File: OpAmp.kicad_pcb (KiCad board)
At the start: 2 copper layers, 47.5 x 26.5 mm, 47 parts, among them J1 Conn_01x05, J2 Conn_01x02, J3 Conn_01x02, J4 Conn_01x02, Q1 5551, Q10 5401, Q11 5551, Q12 5551, Q13 5551, Q14 5401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

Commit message: JLCPCB order 2021-04-11
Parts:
- removed C5: 100 nF, Capacitors_SMD:C_0805_HandSoldering
- removed D1, D2: D_x2_Serial_AKC, TO_SOT_Packages_SMD:SOT-23
- removed Q3, Q6: 5551, TO_SOT_Packages_SMD:SOT-23
- added R14: 680R, Resistors_SMD:R_0805_HandSoldering, F.Cu at (67.5, 70.2)
- added R15: 680R, Resistors_SMD:R_0805_HandSoldering, F.Cu at (62.4, 70.2)
- R2: value 330R -> 680R
- RV1: value 1k -> 2k
- moved Q8 5.08 mm to (72.3, 65.7)
- moved R6 4.99 mm to (72.6, 68.5), turned to 0 degrees
- moved R8 3.83 mm to (76.2, 61.5)
- moved Q10 3.68 mm to (77.5, 65.7), turned to 270 degrees
- moved Q1 3.50 mm to (67.0, 65.8)
- moved Q7 3.45 mm to (63.2, 65.8)
- moved R5 3.02 mm to (79.5, 61.5)
- moved R9 2.85 mm to (82.2, 66.8), turned to 0 degrees
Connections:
- Q1 pad 3: Net-(Q1-Pad3) -> Net-(C7-Pad1)
- Q7 pad 3: Net-(Q6-Pad2) -> Net-(Q2-Pad1)
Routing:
- net VCC: track 65.3 -> 45.9 mm, vias 12 -> 10
- net Net-(C5-Pad2): track 12.8 -> 0.00 mm
- net Net-(Q4-Pad3): track 5.46 -> 11.7 mm
- net Net-(Q7-Pad2): track 4.32 -> 10.0 mm
- net Net-(C7-Pad1): track 28.8 -> 34.0 mm
- net Net-(Q1-Pad2): track 3.75 -> 8.67 mm
- net Net-(C6-Pad1): track 21.3 -> 25.3 mm, vias 2 -> 0
- net Net-(Q10-Pad2): track 5.46 -> 1.94 mm
- net /NEG: track 13.9 -> 11.6 mm
- net VEE: track 46.0 -> 44.0 mm, vias 13 -> 12
- net /POS: track 16.4 -> 14.4 mm
- net Net-(Q6-Pad2): track 1.96 -> 0.00 mm
- net Net-(Q1-Pad3): track 1.91 -> 0.00 mm
- net Net-(D1-Pad2): track 1.89 -> 0.00 mm
- net Net-(Q12-Pad1): track 7.80 -> 8.88 mm
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
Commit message: Added partial outputs
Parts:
- removed J4: Conn_01x02, Pin_Headers:Pin_Header_Straight_1x02_Pitch2.54mm
- J1: value Conn_01x05 -> Conn_01x07; footprint Pin_Headers:Pin_Header_Straight_1x05_Pitch2.54mm -> Pin_Headers:Pin_Header_Straight_1x07_Pitch2.54mm
- moved R12 3.81 mm to (85.2, 79.0), turned to 90 degrees
- moved Q14 2.22 mm to (88.5, 78.7)
- moved Q16 1.32 mm to (79.5, 79.2)
- moved R13 0.66 mm to (82.8, 79.0), turned to 270 degrees
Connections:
- Q15 pad 2: Net-(Q15-Pad2) -> /DRVPLUS
- Q16 pad 2: Net-(J4-Pad2) -> /DRVMINUS
- R12 pad 1: Net-(Q15-Pad2) -> /DRVPLUS
- R13 pad 2: Net-(J4-Pad2) -> /DRVMINUS
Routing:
- net /DRVPLUS: track 0.00 -> 43.7 mm
- net /DRVMINUS: track 0.00 -> 41.0 mm
- net Net-(J4-Pad2): track 8.04 -> 0.00 mm
- net VEE: track 44.0 -> 37.8 mm
- net Net-(Q15-Pad2): track 5.23 -> 0.00 mm
- net /OUT: track 49.0 -> 44.4 mm
- net Net-(C6-Pad2): track 23.4 -> 24.2 mm
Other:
- board size 47.5 x 26.5 mm -> 48 x 28 mm
- board text added: "D+"
- board text added: "D-"

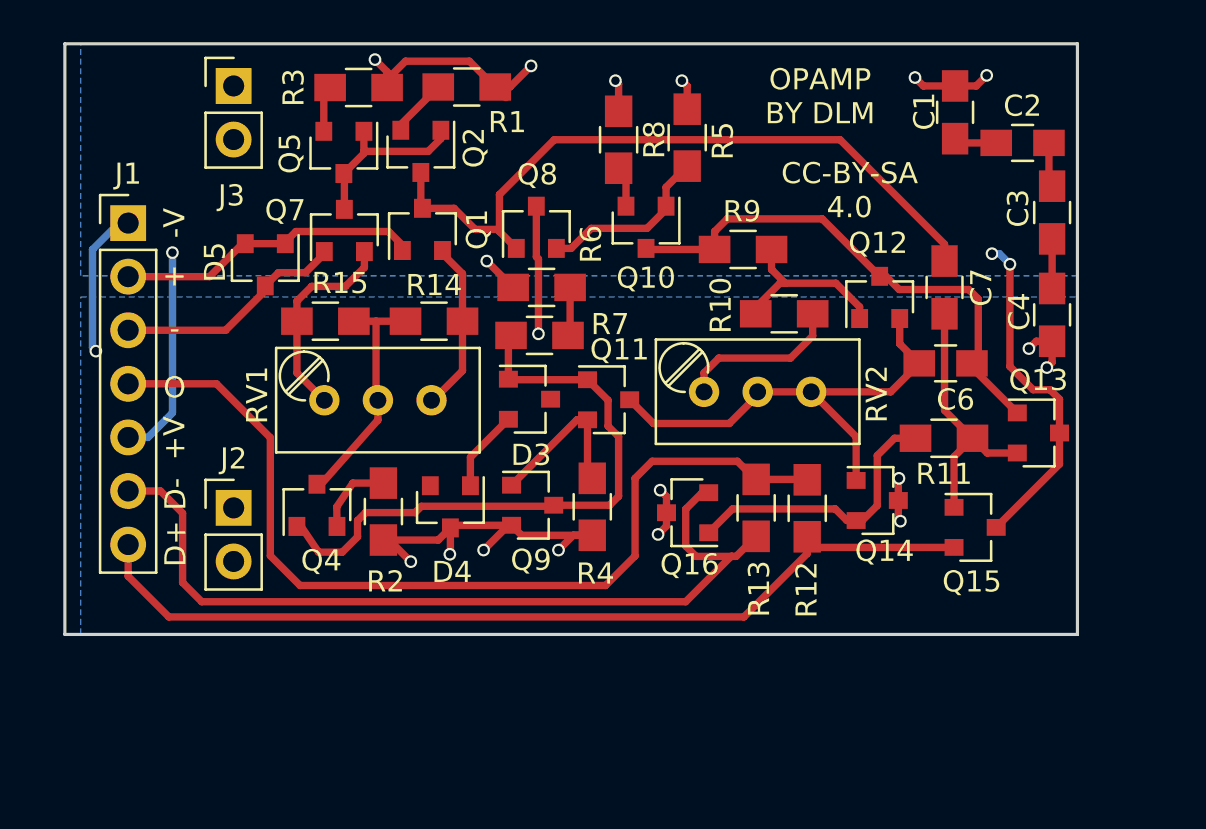
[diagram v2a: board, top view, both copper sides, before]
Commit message: Add spot for power transistors
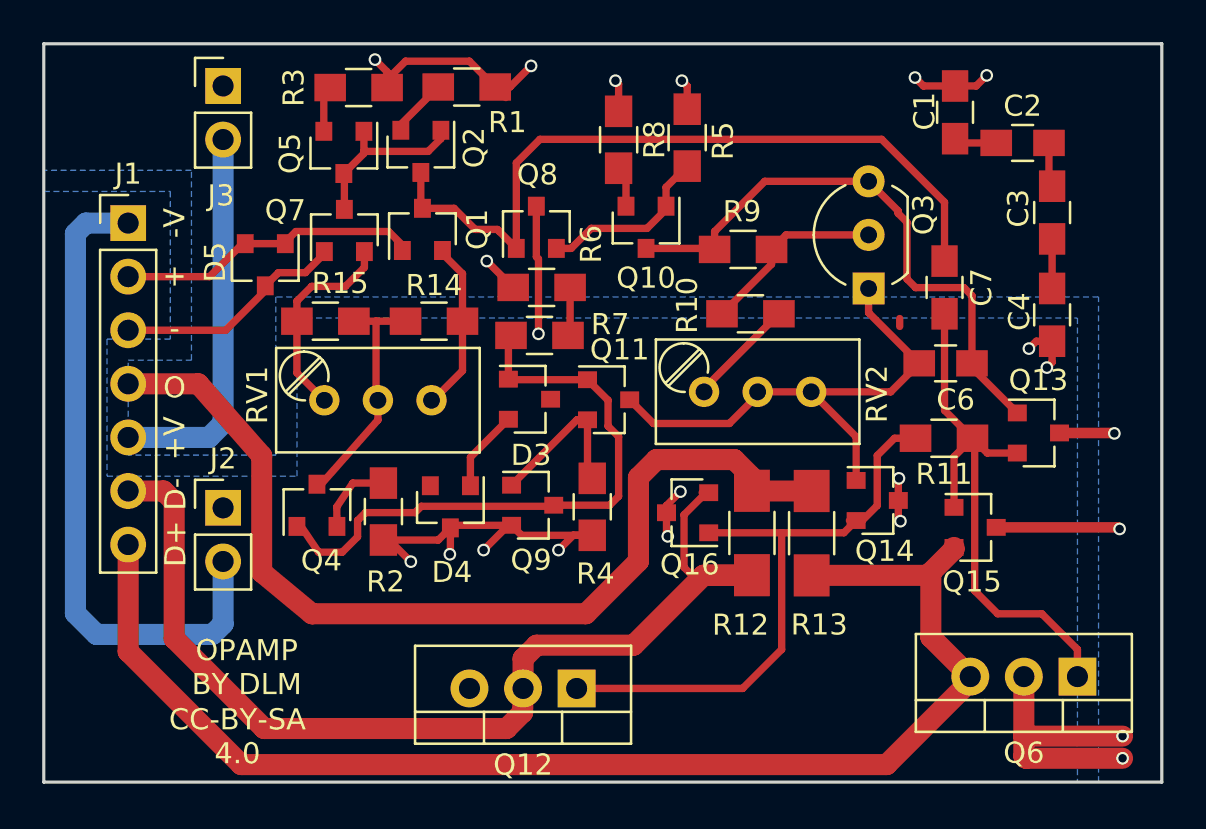
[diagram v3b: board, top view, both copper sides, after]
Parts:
- added Q3: 2N3904, TO_SOT_Packages_THT:TO-92_Inline_Wide, F.Cu at (88.1, 68.6)
- added Q6: TIP41, TO_SOT_Packages_THT:TO-220-3_Vertical, F.Cu at (98.0, 87.0)
- Q12: value 5551 -> TIP42; footprint TO_SOT_Packages_SMD:SOT-23 -> TO_SOT_Packages_THT:TO-220-3_Vertical
- R12, R13: footprint Resistors_SMD:R_0805_HandSoldering -> Resistors_SMD:R_1206_HandSoldering
- moved Q12 23.4 mm to (74.3, 87.6), turned to 180 degrees
- moved R10 1.60 mm to (82.5, 69.8)
- moved R13 1.21 mm to (82.6, 80.2)
- moved R12 1.20 mm to (85.4, 80.2)
- moved J2 0.50 mm to (57.5, 79.0)
- moved J3 0.50 mm to (57.5, 59.0)
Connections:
- Q12 pad 2: Net-(C6-Pad2) -> /DRVMINUS
- Q12 pad 3: Net-(C6-Pad1) -> VEE
- Q14 pad 2: Net-(Q14-Pad2) -> Net-(Q12-Pad1)
- Q16 pad 1: Net-(Q14-Pad2) -> Net-(Q12-Pad1)
- R10 pad 1: Net-(Q12-Pad1) -> Net-(Q3-Pad2)
- R11 pad 2: Net-(Q14-Pad2) -> Net-(Q12-Pad1)
- R9 pad 2: Net-(Q12-Pad1) -> Net-(Q3-Pad2)
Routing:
- net VEE: track 37.8 -> 61.6 mm, vias 12 -> 11
- net Net-(Q12-Pad1): track 8.88 -> 30.0 mm
- net /DRVPLUS: track 43.7 -> 62.1 mm
- net Net-(C7-Pad2): track 12.5 -> 27.1 mm
- net Net-(Q14-Pad2): track 13.8 -> 0.00 mm
- net VCC: track 45.9 -> 59.4 mm, vias 10 -> 11
- net /DRVMINUS: track 41.0 -> 50.5 mm
- net Net-(Q3-Pad2): track 0.00 -> 8.91 mm
- net Net-(C6-Pad1): track 25.3 -> 28.4 mm
- net Net-(R10-Pad2): track 8.25 -> 5.27 mm
- net /OUT: track 44.4 -> 46.6 mm
- net Net-(C7-Pad1): track 34.0 -> 36.0 mm
- net Net-(C6-Pad2): track 24.2 -> 26.0 mm
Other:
- board size 48 x 28 mm -> 53 x 35 mm

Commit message: JLCPCB manufacturing
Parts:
- moved Q6 0.98 mm to (97.0, 87.1)
- moved Q3 0.47 mm to (88.1, 68.1)
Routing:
- net Net-(C6-Pad1): track 28.4 -> 30.5 mm
- net /DRVPLUS: track 62.1 -> 60.9 mm
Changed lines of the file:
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@@
     (thickness 1.6)
     (drawings 13)
-    (tracks 326)
+    (tracks 331)
     (zones 0)
     (modules 45)
@@
   )
   (setup
-    (last_trace_width 1)
+    (last_trace_width 0.35)
     (user_trace_width 0.35)
     (user_trace_width 0.5)
@@
   )
   (module TO_SOT_Packages_THT:TO-92_Inline_Wide (layer F.Cu)
-    (at 88.1 68.6 90)
+    (at 88.13 68.13 90)
     (descr "TO-92 leads in-line, wide, drill 0.8mm (see NXP sot054_po.pdf)")
     (tags "to-92 sc-43 sc-43a sot54 PA33 transistor")
@@
   )
   (module TO_SOT_Packages_THT:TO-220-3_Vertical (layer F.Cu)
-    (at 98 87 180)
+    (at 97.028 87.122 180)
     (descr "TO-220-3, Vertical, RM 2.54mm")
     (tags "TO-220-3 Vertical RM 2.54mm")
@@
   (segment (start 95.56 90.87) (end 100.14 90.87) (width 1) (layer F.Cu) (net 1))
   (segment (start 95.46 90.77) (end 95.56 90.87) (width 1) (layer F.Cu) (net 1))
-  (segment (start 95.46 87) (end 95.46 89.79) (width 1) (layer F.Cu) (net 1))
+  (segment (start 94.488 87.122) (end 95.46 89.79) (width 1) (layer F.Cu) (net 1) (status 10))
   (via (at 100.14 89.82) (size 0.6) (drill 0.4) (layers F.Cu B.Cu) (net 1))
   (segment (start 95.49 89.82) (end 100.14 89.82) (width 1) (layer F.Cu) (net 1))
@@
   (segment (start 71.175 79.825) (end 68.4 79.825) (width 0.35) (layer F.Cu) (net 5))
   (segment (start 68.4 79.825) (end 68.275 79.95) (width 0.35) (layer F.Cu) (net 5))
+  (segment (start 89.92 66.22) (end 89.92 64.84) (width 0.35) (layer F.Cu) (net 6))
+  (segment (start 89.92 64.84) (end 88.13 63.05) (width 0.35) (layer F.Cu) (net 6))
+  (segment (start 80.8 66.75) (end 80.8 64.83) (width 0.35) (layer F.Cu) (net 6))
+  (segment (start 80.8 64.83) (end 82.58 63.05) (width 0.35) (layer F.Cu) (net 6))
+  (segment (start 82.58 63.05) (end 88.13 63.05) (width 0.35) (layer F.Cu) (net 6))
   (segment (start 93 72.15) (end 93 68.94) (width 0.35) (layer F.Cu) (net 6))
-  (segment (start 89.5 64.92) (end 88.1 63.52) (width 0.35) (layer F.Cu) (net 6))
-  (segment (start 89.5 65.04) (end 89.5 64.92) (width 0.35) (layer F.Cu) (net 6))
-  (segment (start 89.92 65.46) (end 89.5 65.04) (width 0.35) (layer F.Cu) (net 6))
-  (segment (start 89.92 68.15) (end 89.92 65.46) (width 0.35) (layer F.Cu) (net 6))
+  (segment (start 93 68.94) (end 92.62 68.56) (width 0.35) (layer F.Cu) (net 6))
+  (segment (start 92.62 68.56) (end 90.33 68.56) (width 0.35) (layer F.Cu) (net 6))
   (segment (start 90.33 68.56) (end 89.92 68.15) (width 0.35) (layer F.Cu) (net 6))
-  (segment (start 92.62 68.56) (end 90.33 68.56) (width 0.35) (layer F.Cu) (net 6))
-  (segment (start 93 68.94) (end 92.62 68.56) (width 0.35) (layer F.Cu) (net 6))
+  (segment (start 89.92 68.15) (end 89.92 66.22) (width 0.35) (layer F.Cu) (net 6))
+  (segment (start 89.92 66.22) (end 89.92 65.46) (width 0.35) (layer F.Cu) (net 6))
   (segment (start 77.55 66.7) (end 80.75 66.7) (width 0.35) (layer F.Cu) (net 6))
   (segment (start 80.75 66.7) (end 80.8 66.75) (width 0.35) (layer F.Cu) (net 6))
-  (segment (start 80.8 66.75) (end 80.8 65.9) (width 0.35) (layer F.Cu) (net 6))
-  (segment (start 80.8 65.9) (end 83.18 63.52) (width 0.35) (layer F.Cu) (net 6))
-  (segment (start 83.18 63.52) (end 88.1 63.52) (width 0.35) (layer F.Cu) (net 6))
   (segment (start 93 72.15) (end 93.25 72.15) (width 0.35) (layer F.Cu) (net 6))
   (segment (start 93.25 72.15) (end 93.4 72) (width 0.35) (layer F.Cu) (net 6))
@@
   (segment (start 93 72.15) (end 93 72.35) (width 0.35) (layer F.Cu) (net 6))
   (segment (start 93 72.35) (end 95.15 74.5) (width 0.35) (layer F.Cu) (net 6))
-  (segment (start 88.1 68.6) (end 88.1 69.75) (width 0.35) (layer F.Cu) (net 7))
+  (segment (start 88.13 68.13) (end 88.1 69.75) (width 0.35) (layer F.Cu) (net 7) (status 10))
   (segment (start 88.1 69.75) (end 90.5 72.15) (width 0.35) (layer F.Cu) (net 7))
   (segment (start 85.5 73.38) (end 85.38 73.5) (width 0.35) (layer F.Cu) (net 7))
@@
   (segment (start 85.175 73.705) (end 85.38 73.5) (width 0.35) (layer F.Cu) (net 7) (status 30))
   (segment (start 76.775 73.875) (end 76.775 73.95) (width 0.35) (layer F.Cu) (net 7))
-  (segment (start 71.4 66.7) (end 71.4 62.65) (width 0.35) (layer F.Cu) (net 8))
-  (segment (start 91.7 64.51) (end 91.7 67.3) (width 0.35) (layer F.Cu) (net 8))
-  (segment (start 88.72 61.53) (end 91.7 64.51) (width 0.35) (layer F.Cu) (net 8))
-  (segment (start 72.52 61.53) (end 88.72 61.53) (width 0.35) (layer F.Cu) (net 8))
+  (segment (start 91.7 64.77) (end 91.7 64.268) (width 0.35) (layer F.Cu) (net 8))
   (segment (start 71.4 62.65) (end 72.52 61.53) (width 0.35) (layer F.Cu) (net 8))
+  (segment (start 71.4 62.65) (end 71.4 66.7) (width 0.35) (layer F.Cu) (net 8))
+  (segment (start 72.582 61.468) (end 72.52 61.53) (width 0.35) (layer F.Cu) (net 8))
+  (segment (start 88.9 61.468) (end 72.582 61.468) (width 0.35) (layer F.Cu) (net 8))
+  (segment (start 91.7 64.268) (end 88.9 61.468) (width 0.35) (layer F.Cu) (net 8))
+  (segment (start 91.7 64.51) (end 91.7 64.77) (width 0.35) (layer F.Cu) (net 8))
+  (segment (start 91.7 64.77) (end 91.7 67.3) (width 0.35) (layer F.Cu) (net 8))
   (segment (start 66.95 64.8) (end 68.45 64.8) (width 0.35) (layer F.Cu) (net 8))
+  (segment (start 68.45 64.8) (end 69.45 65.8) (width 0.35) (layer F.Cu) (net 8))
+  (segment (start 69.45 65.8) (end 70.5 65.8) (width 0.35) (layer F.Cu) (net 8))
+  (segment (start 70.6 65.9) (end 71.4 66.7) (width 0.35) (layer F.Cu) (net 8))
   (segment (start 70.5 65.8) (end 70.6 65.9) (width 0.35) (layer F.Cu) (net 8))
-  (segment (start 70.6 65.9) (end 71.4 66.7) (width 0.35) (layer F.Cu) (net 8))
-  (segment (start 69.45 65.8) (end 70.5 65.8) (width 0.35) (layer F.Cu) (net 8))
-  (segment (start 68.45 64.8) (end 69.45 65.8) (width 0.35) (layer F.Cu) (net 8))
   (segment (start 66.875 63.1) (end 66.875 64.725) (width 0.35) (layer F.Cu) (net 8))
   (segment (start 66.875 64.725) (end 66.95 64.8) (width 0.35) (layer F.Cu) (net 8))
   (segment (start 66.725 63.25) (end 66.875 63.1) (width 0.35) (layer F.Cu) (net 8))
-  (segment (start 98 87) (end 98 85.71) (width 0.35) (layer F.Cu) (net 9))
-  (segment (start 93.13 82.93) (end 93.13 75.805) (width 0.35) (layer F.Cu) (net 9))
-  (segment (start 94.22 84.02) (end 93.13 82.93) (width 0.35) (layer F.Cu) (net 9))
-  (segment (start 96.31 84.02) (end 94.22 84.02) (width 0.35) (layer F.Cu) (net 9))
-  (segment (start 98 85.71) (end 96.31 84.02) (width 0.35) (layer F.Cu) (net 9))
+  (segment (start 93.13 82.804) (end 93.13 83.224) (width 0.35) (layer F.Cu) (net 9))
+  (segment (start 97.028 84.836) (end 97.028 87.122) (width 0.35) (layer F.Cu) (net 9))
+  (segment (start 96.52 84.328) (end 97.028 84.836) (width 0.35) (layer F.Cu) (net 9))
+  (segment (start 94.234 84.328) (end 96.52 84.328) (width 0.35) (layer F.Cu) (net 9))
+  (segment (start 93.13 83.224) (end 94.234 84.328) (width 0.35) (layer F.Cu) (net 9))
+  (segment (start 93.13 82.93) (end 93.13 82.804) (width 0.35) (layer F.Cu) (net 9))
+  (segment (start 93.13 82.804) (end 93.13 75.805) (width 0.35) (layer F.Cu) (net 9))
   (segment (start 93.13 75.805) (end 93.025 75.7) (width 0.35) (layer F.Cu) (net 9))
   (segment (start 91.7 69.8) (end 91.7 74.375) (width 0.35) (layer F.Cu) (net 9))
@@
   (segment (start 80.21 78.28) (end 80.52 78.28) (width 0.35) (layer F.Cu) (net 28))
   (segment (start 53.22 78.2) (end 53 78.2) (width 0.35) (layer F.Cu) (net 28))
-  (segment (start 92.92 87) (end 92.92 87.21) (width 1) (layer F.Cu) (net 29))
-  (segment (start 92.92 87.21) (end 88.96 91.17) (width 1) (layer F.Cu) (net 29))
+  (segment (start 91.948 87.122) (end 91.948 87.332) (width 1) (layer F.Cu) (net 29) (status 30))
+  (segment (start 91.948 87.332) (end 88.96 91.17) (width 1) (layer F.Cu) (net 29) (status 10))
   (segment (start 53 85.81) (end 53 80.74) (width 1) (layer F.Cu) (net 29))
   (segment (start 58.36 91.17) (end 53 85.81) (width 1) (layer F.Cu) (net 29))
   (segment (start 88.96 91.17) (end 58.36 91.17) (width 1) (layer F.Cu) (net 29))
   (segment (start 91.05 82.06) (end 91.05 85.13) (width 1) (layer F.Cu) (net 29))
-  (segment (start 91.05 85.13) (end 92.92 87) (width 1) (layer F.Cu) (net 29))
+  (segment (start 91.05 85.13) (end 91.948 87.122) (width 1) (layer F.Cu) (net 29) (status 20))
   (segment (start 92.15 80.875) (end 92.15 80.96) (width 1) (layer F.Cu) (net 29))
   (segment (start 92.15 80.96) (end 91.05 82.06) (width 1) (layer F.Cu) (net 29))
   (segment (start 91.05 82.06) (end 90.91 82.2) (width 1) (layer F.Cu) (net 29))
   (segment (start 90.91 82.2) (end 85.4 82.2) (width 1) (layer F.Cu) (net 29))
-  (segment (start 88.1 66.06) (end 84.19 66.06) (width 0.35) (layer F.Cu) (net 30))
+  (segment (start 88.13 65.59) (end 84.19 66.06) (width 0.35) (layer F.Cu) (net 30) (status 10))
   (segment (start 84.19 66.06) (end 83.5 66.75) (width 0.35) (layer F.Cu) (net 30))
   (segment (start 83.5 66.75) (end 83.5 67.45) (width 0.35) (layer F.Cu) (net 30))
@@
     (polygon
       (pts
-        (xy 55 71) (xy 52 71) (xy 52 77.5) (xy 61 77.5) (xy 61 70)
-        (xy 98 70) (xy 98 92) (xy 49 92) (xy 49 64) (xy 55 64)
+        (xy 51.952 71) (xy 52 71) (xy 52 77.5) (xy 61 77.5) (xy 61 70)
+        (xy 98 70) (xy 98 92) (xy 49 92) (xy 49 64) (xy 51.952 64)
       )
     )
@@
       (pts
         (xy 102 92) (xy 99 92) (xy 99 69) (xy 60 69) (xy 60 76.5)
-        (xy 53 76.5) (xy 53 72) (xy 56 72) (xy 56 63) (xy 49 63)
+        (xy 53 76.5) (xy 53 72) (xy 54.984 72) (xy 54.984 63) (xy 49 63)
         (xy 49 57) (xy 102 57)
       )

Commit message: Added VAS safety transistor
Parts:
- added Q17: 5401, TO_SOT_Packages_SMD:SOT-23, F.Cu at (72.1, 61.0)
- moved R1 1.10 mm to (68.0, 59.0)
- moved R3 0.93 mm to (63.0, 59.0)
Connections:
- D3 pad 3: (no net) -> Net-(D3-Pad3)
- D4 pad 2: (no net) -> Net-(D4-Pad2)
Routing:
- net VCC: track 59.5 -> 65.8 mm, vias 11 -> 9
- net Net-(C7-Pad1): track 36.5 -> 40.9 mm
- net Net-(Q10-Pad2): track 1.94 -> 6.28 mm
